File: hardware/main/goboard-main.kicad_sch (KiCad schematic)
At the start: 12 parts, among them J1 USB_C_Receptacle_USB2.0

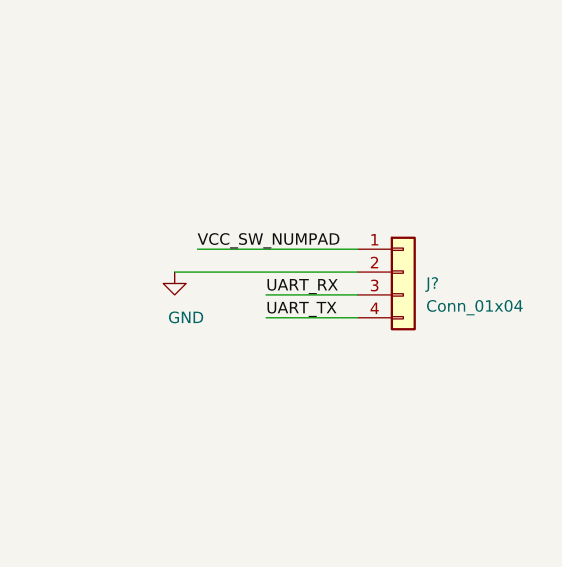
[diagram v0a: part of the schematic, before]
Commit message: Remove UART line from the NRF to the numpad
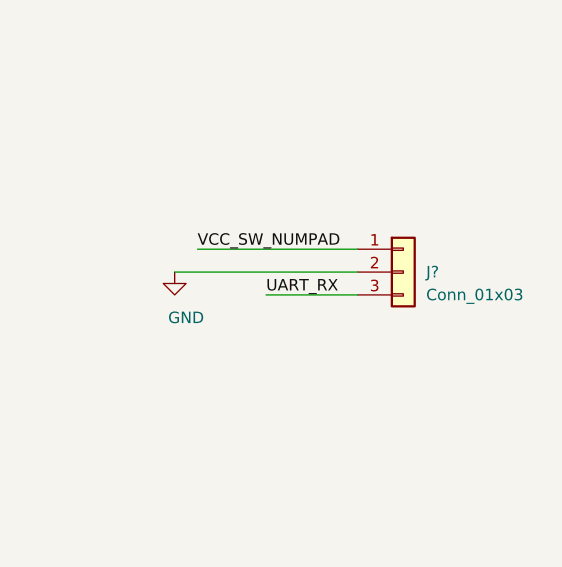
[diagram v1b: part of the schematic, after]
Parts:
- removed J?: Conn_01x04, symbol Connector_Generic:Conn_01x04
- added J?: Conn_01x03, symbol Connector_Generic:Conn_01x03
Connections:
- net GND: now also J?.2 (Pin_2)
- net UART_RX: now also J?.3 (Pin_3)
- net VCC_SW_NUMPAD: now also J?.1 (Pin_1)
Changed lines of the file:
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@@
-    (stroke (width 0) (type solid) (color 0 0 0 0))
-  )
-  (wire (pts (xy 250.19 139.7) (xy 260.35 139.7))
     (stroke (width 0) (type solid) (color 0 0 0 0))
   )
@@
   )
   (label "UART_RX" (at 250.19 137.16 0)
-    (effects (font (size 1.27 1.27)) (justify left bottom))
-  )
-  (label "UART_TX" (at 250.19 139.7 0)
     (effects (font (size 1.27 1.27)) (justify left bottom))
   )
@@
     )
   )
-  (symbol (lib_id "Connector_Generic:Conn_01x04") (at 265.43 134.62 0) (unit 1)
-    (in_bom yes) (on_board yes)
-    (property "Reference" "J?" (id 0) (at 267.97 135.89 0)
-      (effects (font (size 1.27 1.27)) (justify left))
-    )
-    (property "Value" "Conn_01x04" (id 1) (at 267.97 138.43 0)
+  (symbol (lib_id "Connector_Generic:Conn_01x03") (at 265.43 134.62 0) (unit 1)
+    (in_bom yes) (on_board yes)
+    (property "Reference" "J?" (id 0) (at 267.97 134.62 0)
+      (effects (font (size 1.27 1.27)) (justify left))
+    )
+    (property "Value" "Conn_01x03" (id 1) (at 267.97 137.16 0)
       (effects (font (size 1.27 1.27)) (justify left))
     )
@@
       (reference "J?") (unit 1) (value "Conn_02x05_Top_Bottom") (footprint "")
     )
-    (path "/45dbaac3-8890-4544-bcad-241b4dfd7df9"
-      (reference "J?") (unit 1) (value "Conn_01x04") (footprint "")
-    )
     (path "/7892ad65-fd39-49a6-8c1b-cd1bc6d8047e"
       (reference "J?") (unit 1) (value "Conn_01x01") (footprint "")
     )
+    (path "/8f2168b0-9331-41f1-8b2a-0db0627517e9"
+      (reference "J?") (unit 1) (value "Conn_01x03") (footprint "")
+    )
     (path "/70bfc3f4-60ca-4487-a365-ec787e69545b"

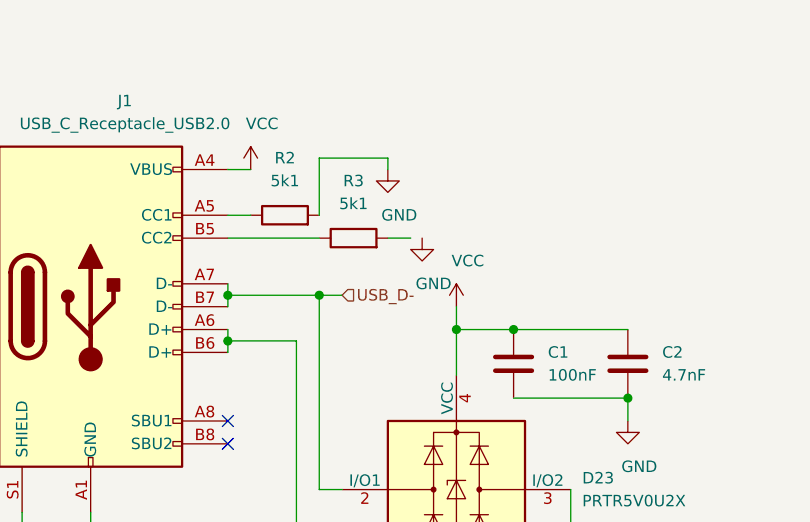
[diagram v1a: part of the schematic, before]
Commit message: Add footprints to many symbols
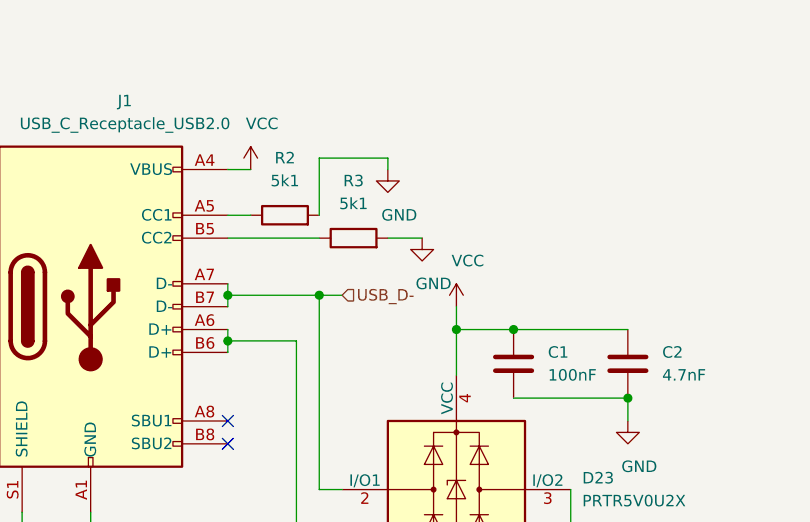
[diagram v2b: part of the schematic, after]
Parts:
- C1, C?: footprint (none) -> Capacitor_SMD:C_0201_0603Metric_Pad0.64x0.40mm_HandSolder; Mouser (none) -> 581-06033C104KAT4A; Part Name (none) -> 06033C104KAT4A
- C2: footprint (none) -> Capacitor_SMD:C_0201_0603Metric_Pad0.64x0.40mm_HandSolder; Mouser (none) -> 77-VJ0603Y472KXACBC; Part Name (none) -> VJ0603Y472KXACW1BC
- D23: Mouser (none) -> 771-PRTR5V0U2X-T/R; Part Name (none) -> PRTR5V0U2X,215
- J?: footprint (none) -> Connector_PinSocket_2.54mm:PinSocket_2x05_P2.54mm_Vertical
- J?: footprint (none) -> Connector_PinHeader_2.54mm:PinHeader_1x01_P2.54mm_Vertical
- R1, R2, R3: footprint (none) -> Resistor_SMD:R_0603_1608Metric_Pad0.98x0.95mm_HandSolder
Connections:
- net GND: now also R3.2

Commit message: Add annotations
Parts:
- gave numbers to parts that had none: 5
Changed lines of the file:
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@@
   (symbol (lib_id "power:VCC") (at 21.59 167.64 0) (unit 1)
     (in_bom yes) (on_board yes)
-    (property "Reference" "#PWR?" (id 0) (at 21.59 171.45 0)
+    (property "Reference" "#PWR0115" (id 0) (at 21.59 171.45 0)
       (effects (font (size 1.27 1.27)) hide)
     )
@@
   (symbol (lib_id "power:VCC") (at 55.88 167.64 0) (unit 1)
     (in_bom yes) (on_board yes)
-    (property "Reference" "#PWR?" (id 0) (at 55.88 171.45 0)
+    (property "Reference" "#PWR0116" (id 0) (at 55.88 171.45 0)
       (effects (font (size 1.27 1.27)) hide)
     )
@@
   (symbol (lib_id "power:GND") (at 21.59 172.72 0) (unit 1)
     (in_bom yes) (on_board yes)
-    (property "Reference" "#PWR?" (id 0) (at 21.59 179.07 0)
+    (property "Reference" "#PWR0114" (id 0) (at 21.59 179.07 0)
       (effects (font (size 1.27 1.27)) hide)
     )
@@
   (symbol (lib_id "power:GND") (at 55.88 172.72 0) (unit 1)
     (in_bom yes) (on_board yes)
-    (property "Reference" "#PWR?" (id 0) (at 55.88 179.07 0)
+    (property "Reference" "#PWR0119" (id 0) (at 55.88 179.07 0)
       (effects (font (size 1.27 1.27)) hide)
     )
@@
   (symbol (lib_id "power:GND") (at 71.12 184.15 0) (unit 1)
     (in_bom yes) (on_board yes)
-    (property "Reference" "#PWR?" (id 0) (at 71.12 190.5 0)
+    (property "Reference" "#PWR0118" (id 0) (at 71.12 190.5 0)
       (effects (font (size 1.27 1.27)) hide)
     )
@@
   (symbol (lib_id "power:GND") (at 88.9 173.99 0) (unit 1)
     (in_bom yes) (on_board yes)
-    (property "Reference" "#PWR?" (id 0) (at 88.9 180.34 0)
+    (property "Reference" "#PWR0117" (id 0) (at 88.9 180.34 0)
       (effects (font (size 1.27 1.27)) hide)
     )
@@
   (symbol (lib_id "power:GND") (at 240.03 134.62 0) (unit 1)
     (in_bom yes) (on_board yes)
-    (property "Reference" "#PWR?" (id 0) (at 240.03 140.97 0)
+    (property "Reference" "#PWR0120" (id 0) (at 240.03 140.97 0)
       (effects (font (size 1.27 1.27)) hide)
     )
@@
   (symbol (lib_id "Connector_Generic:Conn_01x01") (at 38.1 189.23 0) (unit 1)
     (in_bom yes) (on_board yes)
-    (property "Reference" "J?" (id 0) (at 40.64 189.23 0)
+    (property "Reference" "J3" (id 0) (at 40.64 189.23 0)
       (effects (font (size 1.27 1.27)) (justify left))
     )
@@
   (symbol (lib_id "Device:C") (at 71.12 177.8 0) (unit 1)
     (in_bom yes) (on_board yes)
-    (property "Reference" "C?" (id 0) (at 74.93 176.53 0)
+    (property "Reference" "C7" (id 0) (at 74.93 176.53 0)
       (effects (font (size 1.27 1.27)) (justify left))
     )
@@
   (symbol (lib_id "Switch:SW_Push") (at 78.74 173.99 0) (unit 1)
     (in_bom yes) (on_board yes)
-    (property "Reference" "SW?" (id 0) (at 78.74 166.37 0))
+    (property "Reference" "SW11" (id 0) (at 78.74 166.37 0))
     (property "Value" "SW_Push" (id 1) (at 78.74 168.91 0))
     (property "Footprint" "" (id 2) (at 78.74 168.91 0)
@@
   (symbol (lib_id "Connector_Generic:Conn_01x03") (at 265.43 134.62 0) (unit 1)
     (in_bom yes) (on_board yes)
-    (property "Reference" "J?" (id 0) (at 267.97 134.62 0)
+    (property "Reference" "J4" (id 0) (at 267.97 134.62 0)
       (effects (font (size 1.27 1.27)) (justify left))
     )
@@
   (symbol (lib_id "Connector_Generic:Conn_02x05_Top_Bottom") (at 38.1 170.18 0) (mirror x) (unit 1)
     (in_bom yes) (on_board yes)
-    (property "Reference" "J?" (id 0) (at 39.37 181.61 0))
+    (property "Reference" "J2" (id 0) (at 39.37 181.61 0))
     (property "Value" "Conn_02x05_Top_Bottom" (id 1) (at 39.37 179.07 0))
     (property "Footprint" "Connector_PinSocket_2.54mm:PinSocket_2x05_P2.54mm_Vertical" (id 2) (at 38.1 170.18 0)
@@
       (reference "#PWR0108") (unit 1) (value "VCC") (footprint "")
     )
+    (path "/3cca0c92-7d8e-49df-9010-76c61e46cb74"
+      (reference "#PWR0114") (unit 1) (value "GND") (footprint "")
+    )
+    (path "/e1a5293e-3487-44e5-9f3a-714fd6e7f88c"
+      (reference "#PWR0115") (unit 1) (value "VCC") (footprint "")
+    )
+    (path "/5d8ac5ba-d12b-49f1-8a83-545757fd38e6"
+      (reference "#PWR0116") (unit 1) (value "VCC") (footprint "")
+    )
+    (path "/75356a8b-36c6-4cab-8e48-aa1d13fe71cb"
+      (reference "#PWR0117") (unit 1) (value "GND") (footprint "")
+    )
+    (path "/8dcd1007-1f44-42fc-8dd0-7005c064165f"
+      (reference "#PWR0118") (unit 1) (value "GND") (footprint "")
+    )
     (path "/1982d23b-d7d2-4dbb-80ea-7153192d82f3"
-      (reference "#PWR?") (unit 1) (value "GND") (footprint "")
-    )
-    (path "/3cca0c92-7d8e-49df-9010-76c61e46cb74"
-      (reference "#PWR?") (unit 1) (value "GND") (footprint "")
-    )
-    (path "/5d8ac5ba-d12b-49f1-8a83-545757fd38e6"
-      (reference "#PWR?") (unit 1) (value "VCC") (footprint "")
-    )
-    (path "/75356a8b-36c6-4cab-8e48-aa1d13fe71cb"
-      (reference "#PWR?") (unit 1) (value "GND") (footprint "")
-    )
-    (path "/8dcd1007-1f44-42fc-8dd0-7005c064165f"
-      (reference "#PWR?") (unit 1) (value "GND") (footprint "")
+      (reference "#PWR0119") (unit 1) (value "GND") (footprint "")
     )
     (path "/b53f266a-100b-4c6f-9ed7-0ad25cdc4b2e"
-      (reference "#PWR?") (unit 1) (value "GND") (footprint "")
-    )
-    (path "/e1a5293e-3487-44e5-9f3a-714fd6e7f88c"
-      (reference "#PWR?") (unit 1) (value "VCC") (footprint "")
+      (reference "#PWR0120") (unit 1) (value "GND") (footprint "")
     )
     (path "/d7e33325-4578-4e92-bf2f-a87bebb610ba"
@@
     )
     (path "/46b28828-c4d5-4d44-b72d-065b9fca5435"
-      (reference "C?") (unit 1) (value "0,1u") (footprint "Capacitor_SMD:C_0201_0603Metric_Pad0.64x0.40mm_HandSolder")
+      (reference "C7") (unit 1) (value "0,1u") (footprint "Capacitor_SMD:C_0201_0603Metric_Pad0.64x0.40mm_HandSolder")
     )
     (path "/2adac2cc-08ff-4247-86e1-66dd7b51cf23"
@@
     )
     (path "/4449882c-1b7b-492e-9599-d2387f3dd75d"
-      (reference "J?") (unit 1) (value "Conn_02x05_Top_Bottom") (footprint "Connector_PinSocket_2.54mm:PinSocket_2x05_P2.54mm_Vertical")
+      (reference "J2") (unit 1) (value "Conn_02x05_Top_Bottom") (footprint "Connector_PinSocket_2.54mm:PinSocket_2x05_P2.54mm_Vertical")
     )
     (path "/7892ad65-fd39-49a6-8c1b-cd1bc6d8047e"
-      (reference "J?") (unit 1) (value "Conn_01x01") (footprint "Connector_PinHeader_2.54mm:PinHeader_1x01_P2.54mm_Vertical")
+      (reference "J3") (unit 1) (value "Conn_01x01") (footprint "Connector_PinHeader_2.54mm:PinHeader_1x01_P2.54mm_Vertical")
     )
     (path "/8f2168b0-9331-41f1-8b2a-0db0627517e9"
-      (reference "J?") (unit 1) (value "Conn_01x03") (footprint "")
+      (reference "J4") (unit 1) (value "Conn_01x03") (footprint "")
     )
     (path "/70bfc3f4-60ca-4487-a365-ec787e69545b"
@@
     )
     (path "/1873808b-4223-4b68-a2dc-9c41f4922320"
-      (reference "SW?") (unit 1) (value "SW_Push") (footprint "")
+      (reference "SW11") (unit 1) (value "SW_Push") (footprint "")
     )
     (path "/d1d7b976-c206-4a6a-bf43-9e0a3d3fc0a5/30c2ac1c-8a76-41a0-94de-8ad0d2ee7b5a"
       (reference "#PWR0109") (unit 1) (value "GND") (footprint "")
     )
+    (path "/d1d7b976-c206-4a6a-bf43-9e0a3d3fc0a5/6aefb866-3f31-45fc-835d-9e0d0ee3041d"
+      (reference "#PWR0121") (unit 1) (value "GND") (footprint "")
+    )
+    (path "/d1d7b976-c206-4a6a-bf43-9e0a3d3fc0a5/ac41e8bc-33f1-480a-9578-3f27442f4e39"
+      (reference "#PWR0122") (unit 1) (value "GND") (footprint "")
+    )
     (path "/d1d7b976-c206-4a6a-bf43-9e0a3d3fc0a5/456c5560-5e5c-458e-a7f7-e577da6fbd17"
-      (reference "#PWR?") (unit 1) (value "GND") (footprint "")
+      (reference "#PWR0123") (unit 1) (value "GND") (footprint "")
     )
     (path "/d1d7b976-c206-4a6a-bf43-9e0a3d3fc0a5/5d0f01e6-3cac-4a3c-9bd2-0ba422ba5ad9"
-      (reference "#PWR?") (unit 1) (value "GND") (footprint "")
-    )
-    (path "/d1d7b976-c206-4a6a-bf43-9e0a3d3fc0a5/6aefb866-3f31-45fc-835d-9e0d0ee3041d"
-      (reference "#PWR?") (unit 1) (value "GND") (footprint "")
-    )
-    (path "/d1d7b976-c206-4a6a-bf43-9e0a3d3fc0a5/ac41e8bc-33f1-480a-9578-3f27442f4e39"
-      (reference "#PWR?") (unit 1) (value "GND") (footprint "")
+      (reference "#PWR0124") (unit 1) (value "GND") (footprint "")
     )
     (path "/d1d7b976-c206-4a6a-bf43-9e0a3d3fc0a5/2bc4c02f-f267-4fd2-b578-aeec91a0ef1e"

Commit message: Add specialized connector for the programming port
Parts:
- J2: footprint Connector_PinSocket_2.54mm:PinSocket_2x05_P2.54mm_Vertical -> footprints:programming_port_st_link_clone
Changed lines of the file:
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@@
   (junction (at 86.36 60.96) (diameter 1.016) (color 0 0 0 0))
   (no_connect (at 33.02 170.18))
+  (no_connect (at 41.91 63.5))
   (no_connect (at 41.91 66.04))
   (no_connect (at 33.02 165.1))
   (no_connect (at 45.72 165.1))
-  (no_connect (at 41.91 63.5))
   (wire (pts (xy 19.05 73.66) (xy 19.05 76.2))
     (stroke (width 0) (type solid) (color 0 0 0 0))
@@
     (property "Reference" "J2" (id 0) (at 39.37 181.61 0))
     (property "Value" "Conn_02x05_Top_Bottom" (id 1) (at 39.37 179.07 0))
-    (property "Footprint" "Connector_PinSocket_2.54mm:PinSocket_2x05_P2.54mm_Vertical" (id 2) (at 38.1 170.18 0)
+    (property "Footprint" "footprints:programming_port_st_link_clone" (id 2) (at 38.1 170.18 0)
       (effects (font (size 1.27 1.27)) hide)
     )
@@
     )
     (path "/4449882c-1b7b-492e-9599-d2387f3dd75d"
-      (reference "J2") (unit 1) (value "Conn_02x05_Top_Bottom") (footprint "Connector_PinSocket_2.54mm:PinSocket_2x05_P2.54mm_Vertical")
+      (reference "J2") (unit 1) (value "Conn_02x05_Top_Bottom") (footprint "footprints:programming_port_st_link_clone")
     )
     (path "/7892ad65-fd39-49a6-8c1b-cd1bc6d8047e"
